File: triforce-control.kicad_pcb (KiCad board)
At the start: 2 copper layers, 75 x 86 mm, 15 parts, among them CON1 Conn_01x08, CON2 Conn_01x08, CON3 CON_ESC_W1, CON4 CON_ESC_W2, CON5 CON_ESC_W3, CON6 CON_ESC_D1, CON7 CON_ESC_D2, CON8 CON_ESC_D3, CON9 Conn_01x04, U1 ADAFRUIT_HUZZAH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

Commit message: Moved some tracks.
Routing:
- net GND: track 187.1 -> 188.6 mm

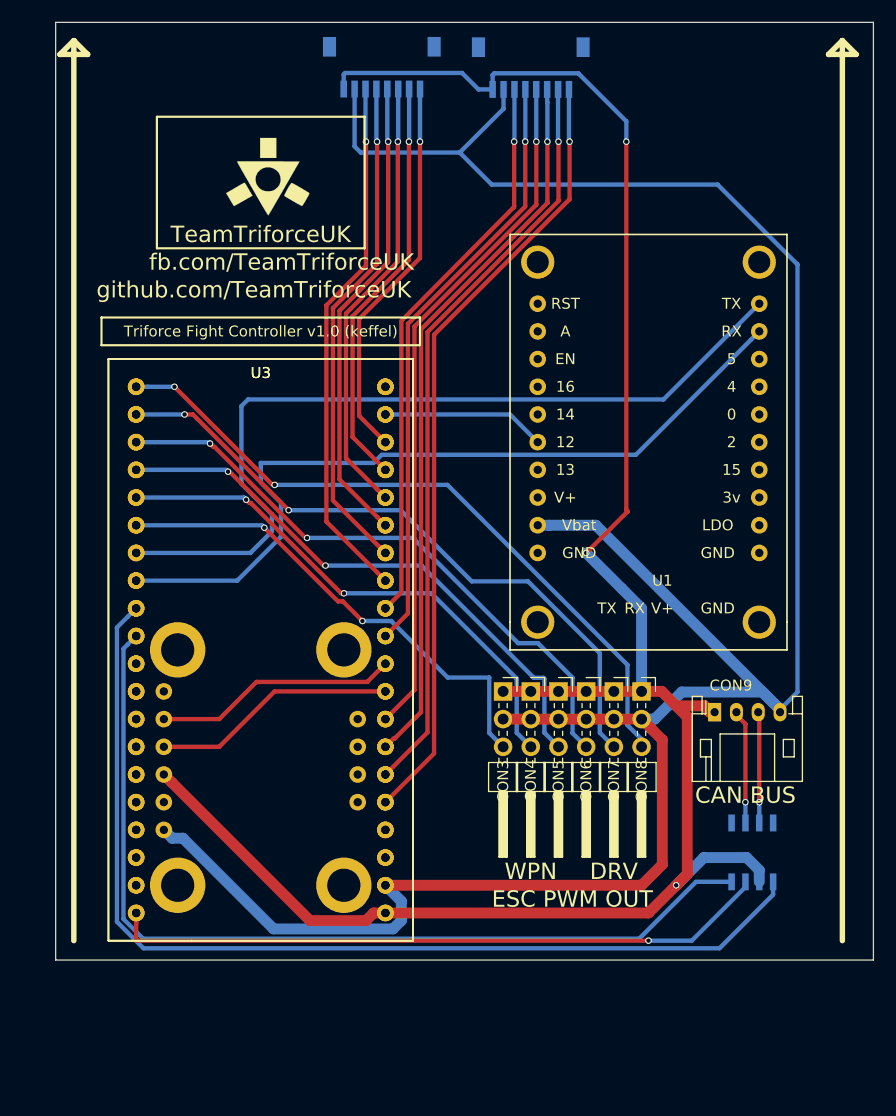
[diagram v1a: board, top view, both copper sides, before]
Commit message: Added silkscreen art.
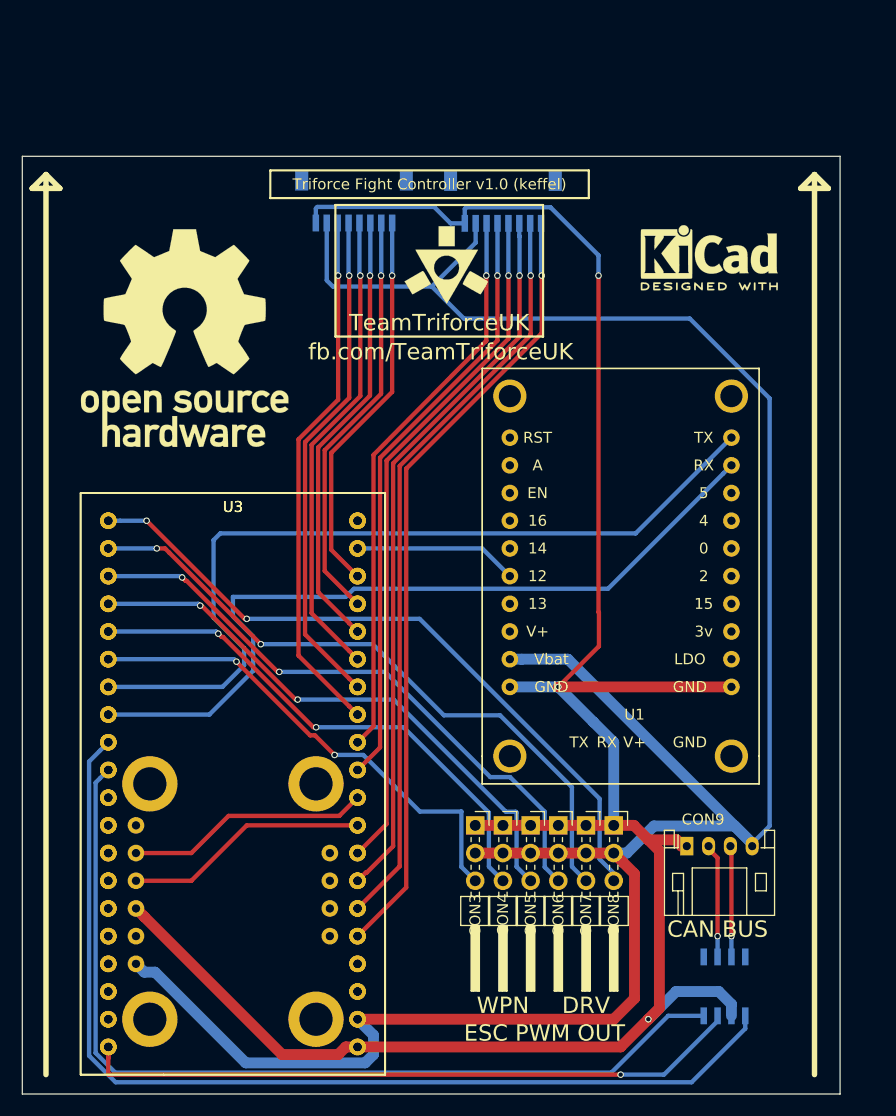
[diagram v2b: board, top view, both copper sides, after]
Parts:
- added REF**: Symbol_CreativeCommonsPublicDomain_SilkScreenTop_Small, Symbols:Symbol_CreativeCommonsPublicDomain_SilkScreenTop_Small, B.Cu at (148.7, 69.7)
- added REF***: KiCad-Logo2_6mm_SilkScreen, Symbols:KiCad-Logo2_6mm_SilkScreen, F.Cu at (175.1, 62.5)
- added REF***: OSHW-Logo_19x20mm_SilkScreen, Symbols:OSHW-Logo_19x20mm_SilkScreen, F.Cu at (127.0, 69.8)
- moved G*** 18.3 mm to (151.0, 63.3)
- moved CON1 12.5 mm to (142.5, 57.3)
- moved CON2 12.5 mm to (156.2, 57.4)
- moved CON3 12.5 mm to (153.7, 117.1)
- moved CON4 12.5 mm to (156.2, 117.1)
- moved CON5 12.5 mm to (158.7, 117.1)
- moved CON6 12.5 mm to (161.3, 117.1)
- moved CON7 12.5 mm to (163.8, 117.1)
- moved CON8 12.5 mm to (166.4, 117.1)
- moved CON9 12.5 mm to (173.1, 116.4)
- moved U1 12.5 mm to (161.9, 76.4)
- moved U2 12.5 mm to (122.5, 127.2)
- moved U3 12.5 mm to (145.4, 84.0) (x2)
- moved U4 12.5 mm to (176.5, 129.3)
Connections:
- U1 pad 11: Net-(U1-Pad11) -> GND
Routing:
- net GND: track 188.6 -> 208.8 mm
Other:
- board text removed: "github.com/TeamTriforceUK"

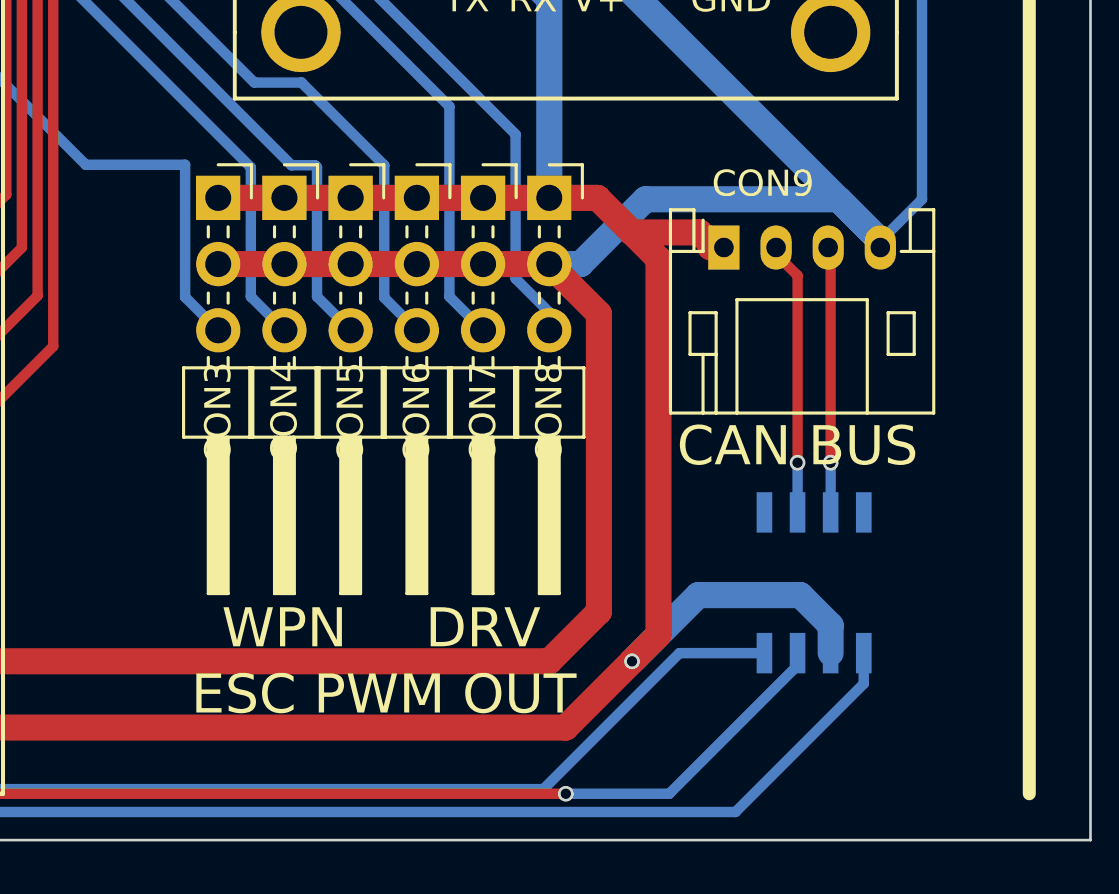
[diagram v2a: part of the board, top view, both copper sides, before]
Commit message: Added boundary boxes on silkscreen for connector blocks.
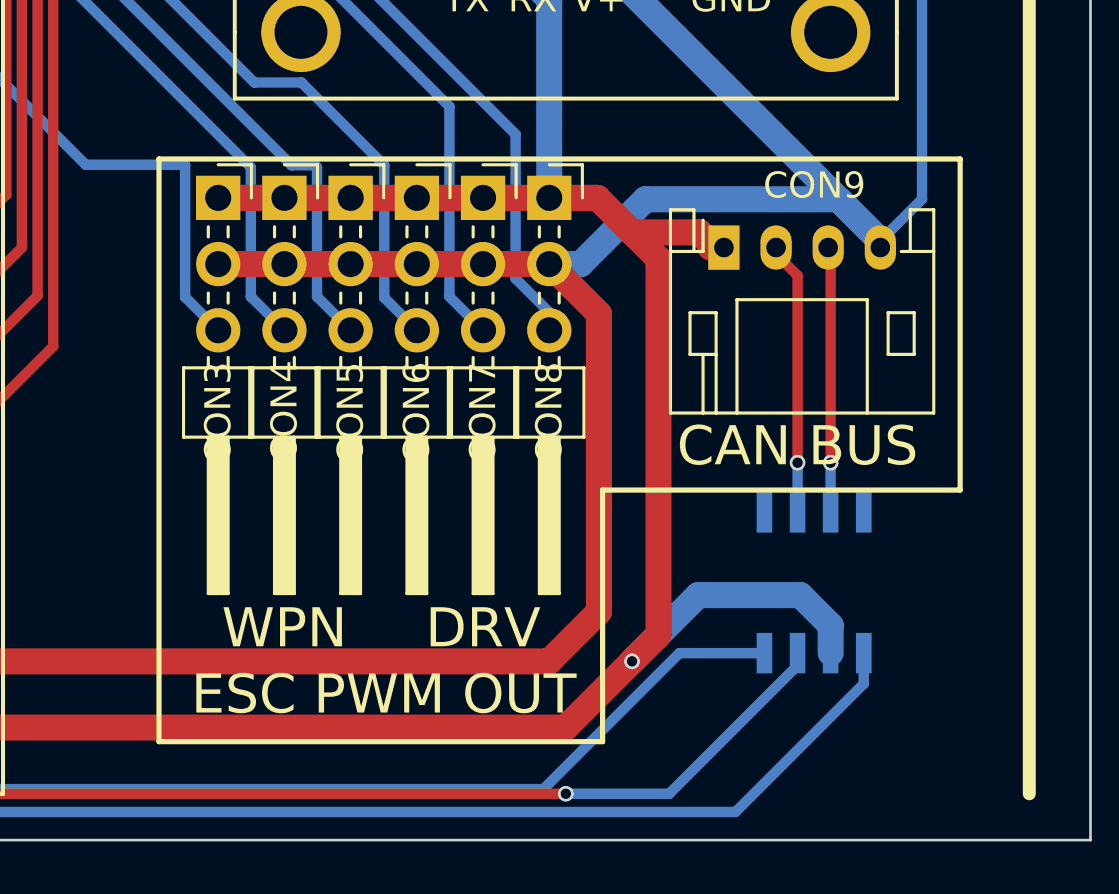
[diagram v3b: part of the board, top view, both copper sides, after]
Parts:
- renumbered REF** to ?
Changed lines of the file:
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@@
     (area 112.068999 53.108999 187.169001 139.209001)
     (thickness 1.6)
-    (drawings 38)
+    (drawings 48)
     (tracks 312)
     (zones 0)
@@
     (descr "JST PH series connector, S4B-PH-K, side entry type, through hole, Datasheet: http://www.jst-mfg.com/product/pdf/eng/ePH.pdf")
     (tags "connector jst ph")
-    (fp_text reference CON9 (at 1.5 -2.45) (layer F.SilkS)
+    (fp_text reference CON9 (at 3.474 -2.38) (layer F.SilkS)
       (effects (font (size 1 1) (thickness 0.15)))
     )
@@
     (descr "Symbol, Creative Commons Public Domain, SilkScreenTop, Small,")
     (tags "Symbol, Creative Commons Public Domain, SilkScreen Top, Small,")
-    (fp_text reference REF** (at 0.59944 7.29996 180) (layer B.SilkS)
+    (fp_text reference "" (at 0.59944 7.29996 180) (layer B.SilkS)
       (effects (font (size 1 1) (thickness 0.15)) (justify mirror))
     )
@@
     (fp_line (start -13.15056 2.3003) (end -13.75 2.39936) (layer B.SilkS) (width 0.15))
   )
+  (gr_line (start 136.144 64.516) (end 136.144 53.848) (layer B.SilkS) (width 0.2))
+  (gr_line (start 162.56 64.516) (end 136.144 64.516) (layer B.SilkS) (width 0.2))
+  (gr_line (start 162.56 53.848) (end 162.56 64.516) (layer B.SilkS) (width 0.2))
+  (gr_line (start 136.144 53.848) (end 162.56 53.848) (layer B.SilkS) (width 0.2))
+  (gr_line (start 151.384 113.03) (end 151.384 135.382) (layer F.SilkS) (width 0.2))
+  (gr_line (start 182.118 113.03) (end 151.384 113.03) (layer F.SilkS) (width 0.2))
+  (gr_line (start 182.118 125.73) (end 182.118 113.03) (layer F.SilkS) (width 0.2))
+  (gr_line (start 168.402 125.73) (end 182.118 125.73) (layer F.SilkS) (width 0.2))
+  (gr_line (start 168.402 135.382) (end 168.402 125.73) (layer F.SilkS) (width 0.2))
+  (gr_line (start 151.384 135.382) (end 168.402 135.382) (layer F.SilkS) (width 0.2))
   (gr_line (start 112.119 53.159) (end 112.119 139.159) (layer Edge.Cuts) (width 0.1))
   (gr_line (start 187.119 53.159) (end 112.119 53.159) (layer Edge.Cuts) (width 0.1))

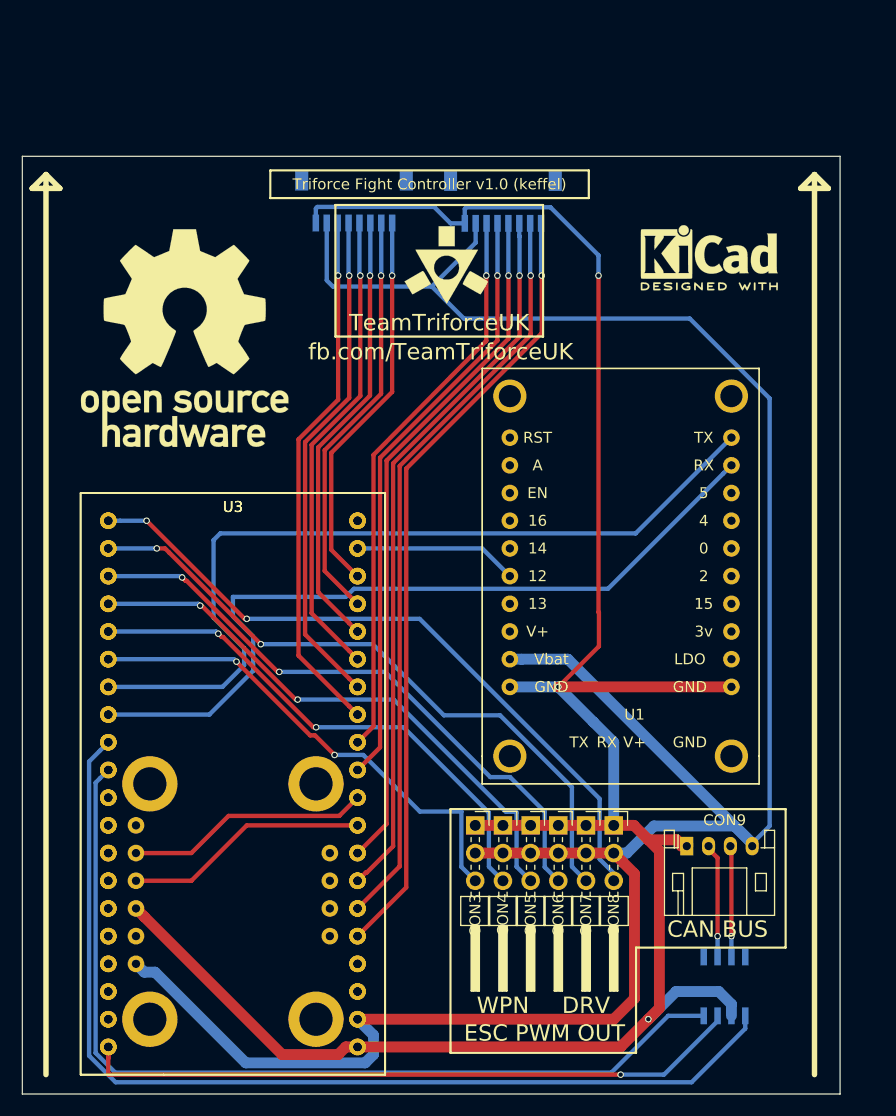
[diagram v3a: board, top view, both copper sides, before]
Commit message: PCB track cleanup and alignment.
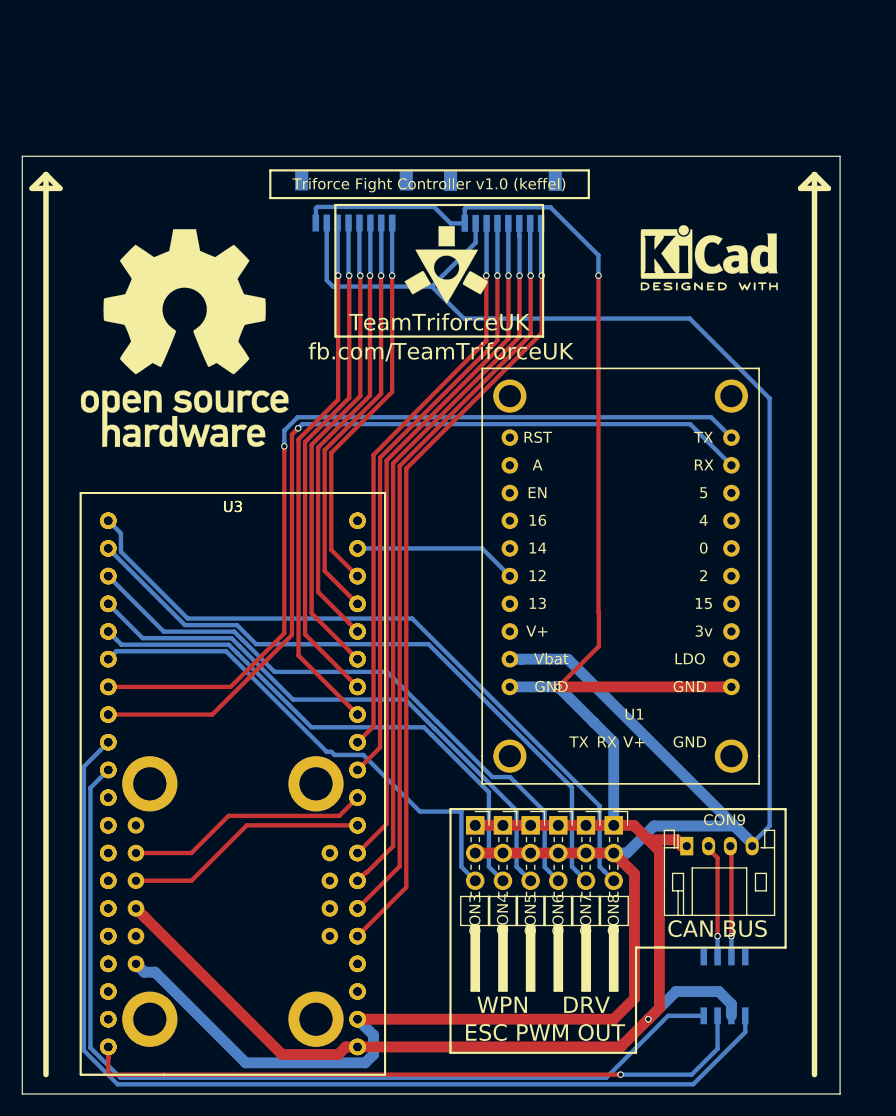
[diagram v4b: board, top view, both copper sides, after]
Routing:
- net ESP_MBED_TX: track 73.2 -> 80.5 mm, vias 0 -> 1
- net ESP_MBED_RX: track 77.3 -> 79.1 mm, vias 0 -> 1
- net MBED_3V3: track 62.0 -> 63.5 mm
- net PWM_OUT_WPN_MOTOR_2: track 48.6 -> 49.7 mm, vias 2 -> 0
- net CAN_RXD: track 85.1 -> 85.9 mm
- net CAN_TXD: track 93.9 -> 94.6 mm
- net PWM_OUT_WPN_MOTOR_1: track 45.0 -> 45.6 mm, vias 2 -> 0
- net PWM_OUT_DRV_MOTOR_3: track 63.9 -> 64.3 mm, vias 2 -> 0
- net PWM_OUT_WPN_MOTOR_3: track 52.2 -> 52.3 mm, vias 2 -> 0
- net PWM_OUT_DRV_MOTOR_2: vias 2 -> 0
- net PWM_OUT_DRV_MOTOR_1: vias 2 -> 0
